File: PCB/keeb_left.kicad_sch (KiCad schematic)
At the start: 0 parts

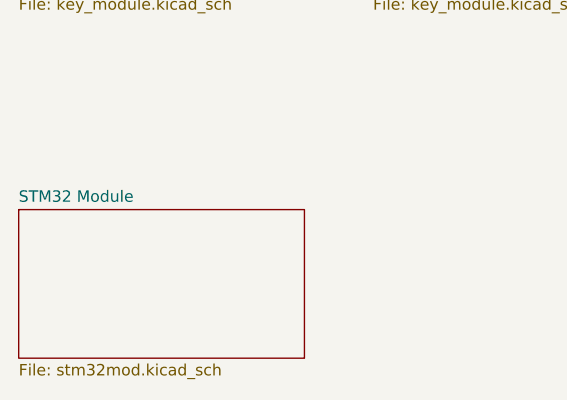
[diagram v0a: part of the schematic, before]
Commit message: Removed stm32, we're using a BluePill instead.
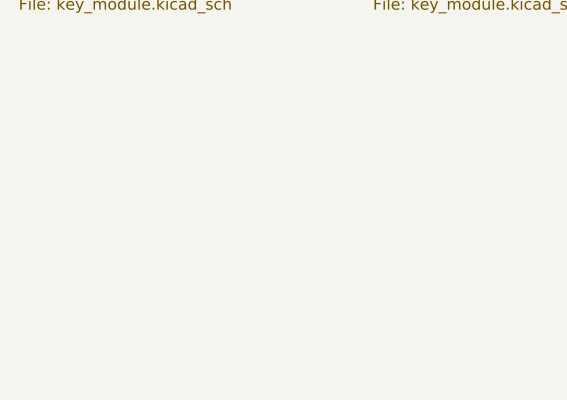
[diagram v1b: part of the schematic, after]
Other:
- removed sheet STM32 Module
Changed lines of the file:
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@@
-    )
-  )
-  (sheet (at 29.21 66.04) (size 31.75 16.51) (fields_autoplaced)
-    (stroke (width 0.1524) (type solid))
-    (fill (color 0 0 0 0.0000))
-    (property "Sheetname" "STM32 Module" (at 29.21 65.3284 0)
-      (effects (font (size 1.27 1.27)) (justify left bottom))
-    )
-    (property "Sheetfile" "stm32mod.kicad_sch" (at 29.21 83.1346 0)
-      (effects (font (size 1.27 1.27)) (justify left top))
-    )
-    (instances
-      (project "PCB"
-        (path "/d2f5552d-48c0-49b0-8e54-6764f47ed1da/5a7a16c1-b018-4a19-b382-77ab07b68c52" (page "54"))
-      )
     )
   )

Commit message: Done with STM32
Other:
- added sheet STM32 Module (stm32mod.kicad_sch)
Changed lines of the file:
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@@
+    (stroke (width 0) (type default))
+  )
+  (wire (pts (xy 49.53 81.28) (xy 25.4 81.28))
+    (stroke (width 0) (type default))
+  )
+  (wire (pts (xy 260.35 46.99) (xy 260.35 39.37))
     (stroke (width 0) (type default))
   )
@@
     (stroke (width 0) (type default))
   )
+  (wire (pts (xy 21.59 31.75) (xy 29.21 31.75))
+    (stroke (width 0) (type default))
+  )
+  (wire (pts (xy 25.4 81.28) (xy 25.4 46.99))
+    (stroke (width 0) (type default))
+  )
   (wire (pts (xy 60.96 31.75) (xy 68.58 31.75))
     (stroke (width 0) (type default))
@@
   )
   (wire (pts (xy 100.33 39.37) (xy 107.95 39.37))
+    (stroke (width 0) (type default))
+  )
+  (wire (pts (xy 21.59 86.36) (xy 21.59 31.75))
+    (stroke (width 0) (type default))
+  )
+  (wire (pts (xy 25.4 46.99) (xy 260.35 46.99))
+    (stroke (width 0) (type default))
+  )
+  (wire (pts (xy 49.53 86.36) (xy 21.59 86.36))
+    (stroke (width 0) (type default))
+  )
+  (wire (pts (xy 260.35 39.37) (xy 257.81 39.37))
     (stroke (width 0) (type default))
   )
@@
       )
     )
+  )
+  (sheet (at 49.53 67.31) (size 38.1 49.53) (fields_autoplaced)
+    (stroke (width 0.1524) (type solid))
+    (fill (color 0 0 0 0.0000))
+    (property "Sheetname" "STM32 Module" (at 49.53 66.5984 0)
+      (effects (font (size 1.27 1.27)) (justify left bottom))
+    )
+    (property "Sheetfile" "stm32mod.kicad_sch" (at 49.53 117.4246 0)
+      (effects (font (size 1.27 1.27)) (justify left top))
+    )
+    (pin "PA0" input (at 49.53 71.12 180)
+      (effects (font (size 1.27 1.27)) (justify left))
+    )
+    (pin "PB4" input (at 49.53 88.9 180)
+      (effects (font (size 1.27 1.27)) (justify left))
+    )
+    (pin "PB3" input (at 49.53 86.36 180)
+      (effects (font (size 1.27 1.27)) (justify left))
+    )
+    (pin "I2C2_SCL" input (at 87.63 83.82 0)
+      (effects (font (size 1.27 1.27)) (justify right))
+    )
+    (pin "I2C2_SDA" input (at 87.63 81.28 0)
+      (effects (font (size 1.27 1.27)) (justify right))
+    )
+    (pin "I2C1_SMBAI" input (at 87.63 76.2 0)
+      (effects (font (size 1.27 1.27)) (justify right))
+    )
+    (pin "PB9" input (at 49.53 93.98 180)
+      (effects (font (size 1.27 1.27)) (justify left))
+    )
+    (pin "PB14" input (at 49.53 99.06 180)
+      (effects (font (size 1.27 1.27)) (justify left))
+    )
+    (pin "PB13" input (at 49.53 96.52 180)
+      (effects (font (size 1.27 1.27)) (justify left))
+    )
+    (pin "PB15" input (at 49.53 101.6 180)
+      (effects (font (size 1.27 1.27)) (justify left))
+    )
+    (pin "I2C1_SCL" input (at 87.63 73.66 0)
+      (effects (font (size 1.27 1.27)) (justify right))
+    )
+    (pin "I2C1_SDA" input (at 87.63 71.12 0)
+      (effects (font (size 1.27 1.27)) (justify right))
+    )
+    (pin "PB8" input (at 49.53 91.44 180)
+      (effects (font (size 1.27 1.27)) (justify left))
+    )
+    (pin "PA15" input (at 49.53 81.28 180)
+      (effects (font (size 1.27 1.27)) (justify left))
+    )
+    (pin "USART1_RX" input (at 87.63 91.44 0)
+      (effects (font (size 1.27 1.27)) (justify right))
+    )
+    (pin "USART1_TX" input (at 87.63 93.98 0)
+      (effects (font (size 1.27 1.27)) (justify right))
+    )
+    (pin "USART1_CK" input (at 87.63 96.52 0)
+      (effects (font (size 1.27 1.27)) (justify right))
+    )
+    (pin "ADC12_IN6" input (at 49.53 111.76 180)
+      (effects (font (size 1.27 1.27)) (justify left))
+    )
+    (pin "ADC12_IN7" input (at 49.53 114.3 180)
+      (effects (font (size 1.27 1.27)) (justify left))
+    )
+    (pin "ADC12_IN4" input (at 49.53 106.68 180)
+      (effects (font (size 1.27 1.27)) (justify left))
+    )
+    (pin "ADC12_IN5" input (at 49.53 109.22 180)
+      (effects (font (size 1.27 1.27)) (justify left))
+    )
+    (pin "PA2" input (at 49.53 76.2 180)
+      (effects (font (size 1.27 1.27)) (justify left))
+    )
+    (pin "PA3" input (at 49.53 78.74 180)
+      (effects (font (size 1.27 1.27)) (justify left))
+    )
+    (pin "PA1" input (at 49.53 73.66 180)
+      (effects (font (size 1.27 1.27)) (justify left))
+    )
+    (pin "I2C2_SMBAI" input (at 87.63 86.36 0)
+      (effects (font (size 1.27 1.27)) (justify right))
+    )
+    (instances
+      (project "PCB"
+        (path "/d2f5552d-48c0-49b0-8e54-6764f47ed1da/5a7a16c1-b018-4a19-b382-77ab07b68c52" (page "54"))
+      )
+    )

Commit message: Ready to work on PCB
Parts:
- added D7: 6V ESD, footprint:SOD-123FL_L2.8-W1.8-LS3.7-BI, symbol JLCPCB:SMF6_0CA_C2990473
- added J1: ALS, Connector_PinHeader_2.54mm:PinHeader_1x03_P2.54mm_Vertical, symbol Connector_Generic:Conn_01x03
- added J1: Serial, Connector_PinHeader_2.54mm:PinHeader_1x05_P2.54mm_Vertical, symbol Connector_Generic:Conn_01x05
- added J1: I2C, Connector_PinHeader_2.54mm:PinHeader_1x04_P2.54mm_Vertical, symbol Connector_Generic:Conn_01x04
- added U44: TYPE-C-31-M-12, footprint:USB-C_SMD-TYPE-C-31-M-12, symbol JLCPCB:TYPE-C-31-M-12
- added U48: USBLC6-2SC6, Package_TO_SOT_SMD:SOT-23-6, symbol Power_Protection:USBLC6-2SC6
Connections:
- net STM32 Module/ADC12_IN4: now also J1.2 (Pin_2)
- net STM32 Module/I2C2_SCL: now also J1.3 (Pin_3)
- net STM32 Module/I2C2_SDA: now also J1.2 (Pin_2)
- net STM32 Module/USART1_CK: now also J1.4 (Pin_4)
- net STM32 Module/USART1_RX: now also J1.2 (Pin_2)
- net STM32 Module/USART1_TX: now also J1.3 (Pin_3)
- new net +5V: J1.3 (Pin_3), U48.5 (VBUS)
- new net GND: D7.1, J1.1 (Pin_1), J1.4 (Pin_4), J1.5 (Pin_5), U44.0 (SH), U44.A1 (GND), U44.A12 (GND), U44.B1 (GND), U44.B12 (GND), U48.2 (GND)
- new net HALF_CONN_C: U44.A5 (CC1), U44.B5 (CC2)
- new net HALF_CONN_N: U44.A7 (DN1), U44.B7 (DN2), U48.1 (I/O1)
- new net HALF_CONN_P: U44.A6 (DP1), U44.B6 (DP2), U48.3 (I/O2)
- new net HALF_CONN_S: U44.A8 (SBU1), U44.B8 (SBU2)
- new net HALF_SCL: U48.4 (I/O2)
- new net HALF_SDA: U48.6 (I/O1)
- new net VBUS: D7.2, J1.1 (Pin_1), J1.1 (Pin_1), U44.A4 (VBUS), U44.A9 (VBUS), U44.B4 (VBUS), U44.B9 (VBUS)
- no-connect marks 0 -> 6
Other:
- sheet STM32 Module ports: added VUSB_RAW; removed none

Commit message: Plugin works.
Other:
- added sheet 5-Key Module1 (key_module_5.kicad_sch)
- note added: "Left-Right Connector"
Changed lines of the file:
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@@
     (stroke (width 0) (type default))
+  )
+  (text "Left-Right Connector" (at 20.32 133.35 0)
+    (effects (font (size 1.27 1.27)) (justify left bottom))
   )
   (label "HALF_CONN_C" (at 24.13 162.56 0) (fields_autoplaced)
@@
         )
         (path "/d2f5552d-48c0-49b0-8e54-6764f47ed1da/5a7a16c1-b018-4a19-b382-77ab07b68c52"
-          (reference "#PWR0227") (unit 1)
+          (reference "#PWR060008") (unit 1)
         )
       )
@@
         )
         (path "/d2f5552d-48c0-49b0-8e54-6764f47ed1da/5a7a16c1-b018-4a19-b382-77ab07b68c52"
-          (reference "#PWR0211") (unit 1)
+          (reference "#PWR060007") (unit 1)
         )
       )
@@
   (symbol (lib_id "power:+5V") (at 114.3 165.1 0) (unit 1)
     (in_bom yes) (on_board yes) (dnp no)
-    (property "Reference" "#PWR0230" (at 114.3 168.91 0)
+    (property "Reference" "#PWR060013" (at 114.3 168.91 0)
       (effects (font (size 1.27 1.27)) hide)
     )
@@
       (project "PCB"
         (path "/d2f5552d-48c0-49b0-8e54-6764f47ed1da/5a7a16c1-b018-4a19-b382-77ab07b68c52"
-          (reference "#PWR0230") (unit 1)
+          (reference "#PWR060013") (unit 1)
         )
       )
@@
   (symbol (lib_id "power:+5V") (at 27.94 101.6 0) (unit 1)
     (in_bom yes) (on_board yes) (dnp no) (fields_autoplaced)
-    (property "Reference" "#PWR0236" (at 27.94 105.41 0)
+    (property "Reference" "#PWR060001" (at 27.94 105.41 0)
       (effects (font (size 1.27 1.27)) hide)
     )
@@
       (project "PCB"
         (path "/d2f5552d-48c0-49b0-8e54-6764f47ed1da/5a7a16c1-b018-4a19-b382-77ab07b68c52"
-          (reference "#PWR0236") (unit 1)
+          (reference "#PWR060001") (unit 1)
         )
       )
@@
         )
         (path "/d2f5552d-48c0-49b0-8e54-6764f47ed1da/5a7a16c1-b018-4a19-b382-77ab07b68c52"
-          (reference "#PWR0229") (unit 1)
+          (reference "#PWR060010") (unit 1)
         )
       )
@@
         )
         (path "/d2f5552d-48c0-49b0-8e54-6764f47ed1da/5a7a16c1-b018-4a19-b382-77ab07b68c52"
-          (reference "#PWR0232") (unit 1)
+          (reference "#PWR060005") (unit 1)
         )
       )
@@
         )
         (path "/d2f5552d-48c0-49b0-8e54-6764f47ed1da/5a7a16c1-b018-4a19-b382-77ab07b68c52"
-          (reference "D3") (unit 1)
+          (reference "D60001") (unit 1)
         )
       )
@@
         )
         (path "/d2f5552d-48c0-49b0-8e54-6764f47ed1da/5a7a16c1-b018-4a19-b382-77ab07b68c52"
-          (reference "#PWR0235") (unit 1)
+          (reference "#PWR060012") (unit 1)
         )
       )
@@
         )
         (path "/d2f5552d-48c0-49b0-8e54-6764f47ed1da/5a7a16c1-b018-4a19-b382-77ab07b68c52"
-          (reference "#PWR0210") (unit 1)
+          (reference "#PWR060004") (unit 1)
         )
       )
@@
         )
         (path "/d2f5552d-48c0-49b0-8e54-6764f47ed1da/5a7a16c1-b018-4a19-b382-77ab07b68c52"
-          (reference "J3") (unit 1)
+          (reference "J60001") (unit 1)
         )
       )
@@
         )
         (path "/d2f5552d-48c0-49b0-8e54-6764f47ed1da/5a7a16c1-b018-4a19-b382-77ab07b68c52"
-          (reference "J4") (unit 1)
+          (reference "J60002") (unit 1)
         )
       )
@@
         )
         (path "/d2f5552d-48c0-49b0-8e54-6764f47ed1da/5a7a16c1-b018-4a19-b382-77ab07b68c52"
-          (reference "J2") (unit 1)
+          (reference "J60003") (unit 1)
         )
       )
@@
         )
         (path "/d2f5552d-48c0-49b0-8e54-6764f47ed1da/5a7a16c1-b018-4a19-b382-77ab07b68c52"
-          (reference "#PWR0231") (unit 1)
+          (reference "#PWR060009") (unit 1)
         )
       )
@@
         )
         (path "/d2f5552d-48c0-49b0-8e54-6764f47ed1da/5a7a16c1-b018-4a19-b382-77ab07b68c52"
-          (reference "#PWR0234") (unit 1)
+          (reference "#PWR060002") (unit 1)
         )
       )
@@
         )
         (path "/d2f5552d-48c0-49b0-8e54-6764f47ed1da/5a7a16c1-b018-4a19-b382-77ab07b68c52"
-          (reference "U50") (unit 1)
+          (reference "U60002") (unit 1)
         )
       )
@@
         )
         (path "/d2f5552d-48c0-49b0-8e54-6764f47ed1da/5a7a16c1-b018-4a19-b382-77ab07b68c52"
-          (reference "U49") (unit 1)
+          (reference "U60001") (unit 1)
         )
       )
@@
         )
         (path "/d2f5552d-48c0-49b0-8e54-6764f47ed1da/5a7a16c1-b018-4a19-b382-77ab07b68c52"
-          (reference "#PWR0209") (unit 1)
+          (reference "#PWR060003") (unit 1)
         )
       )
@@
         )
         (path "/d2f5552d-48c0-49b0-8e54-6764f47ed1da/5a7a16c1-b018-4a19-b382-77ab07b68c52"
-          (reference "#PWR0233") (unit 1)
+          (reference "#PWR060006") (unit 1)
         )
       )
@@
         )
         (path "/d2f5552d-48c0-49b0-8e54-6764f47ed1da/5a7a16c1-b018-4a19-b382-77ab07b68c52"
-          (reference "#PWR0237") (unit 1)
+          (reference "#PWR060011") (unit 1)
         )
       )
@@
       )
     )
+  )
+  (sheet (at 205.74 80.01) (size 31.75 12.7) (fields_autoplaced)
+    (stroke (width 0.1524) (type solid))
+    (fill (color 0 0 0 0.0000))
+    (property "Sheetname" "5-Key Module1" (at 205.74 79.2984 0)
+      (effects (font (size 1.27 1.27)) (justify left bottom))
+    )
+    (property "Sheetfile" "key_module_5.kicad_sch" (at 205.74 93.2946 0)
+      (effects (font (size 1.27 1.27)) (justify left top))
+    )
+    (pin "SR_IN" input (at 205.74 90.17 180)
+      (effects (font (size 1.27 1.27)) (justify left))
+    )
+    (pin "SR_CLOCK" input (at 222.25 80.01 90)
+      (effects (font (size 1.27 1.27)) (justify right))
+    )
+    (pin "SR_LOAD" input (at 219.71 80.01 90)
+      (effects (font (size 1.27 1.27)) (justify right))
+    )
+    (pin "LEDInput" input (at 205.74 82.55 180)
+      (effects (font (size 1.27 1.27)) (justify left))
+    )
+    (pin "SR_OUT" input (at 237.49 90.17 0)
+      (effects (font (size 1.27 1.27)) (justify right))
+    )
+    (pin "LEDOutput" input (at 237.49 82.55 0)
+      (effects (font (size 1.27 1.27)) (justify right))
+    )
+    (instances
+      (project "PCB"
+        (path "/d2f5552d-48c0-49b0-8e54-6764f47ed1da" (page "47"))
+        (path "/d2f5552d-48c0-49b0-8e54-6764f47ed1da/5a7a16c1-b018-4a19-b382-77ab07b68c52" (page "49"))
+      )
+    )

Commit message: Laying out the PCB.
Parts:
- removed J1: Serial, Connector_PinHeader_2.54mm:PinHeader_1x05_P2.54mm_Vertical, symbol Connector_Generic:Conn_01x05
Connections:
- no-connect marks 6 -> 9
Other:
- removed sheet 5-Key Module1
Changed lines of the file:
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@@
   (junction (at 125.73 22.86) (diameter 0) (color 0 0 0 0)
   )
+  (no_connect (at 87.63 93.98))
   (no_connect (at 81.28 170.18))
   (no_connect (at 87.63 86.36))
   (no_connect (at 87.63 76.2))
+  (no_connect (at 87.63 91.44))
   (no_connect (at 257.81 31.75))
+  (no_connect (at 87.63 96.52))
   (no_connect (at 29.21 39.37))
   (no_connect (at 81.28 162.56))
@@
     (stroke (width 0) (type default))
   )
-  (wire (pts (xy 90.17 88.9) (xy 95.25 88.9))
-    (stroke (width 0) (type default))
-  )
   (wire (pts (xy 71.12 172.72) (xy 63.5 172.72))
     (stroke (width 0) (type default))
@@
     (stroke (width 0) (type default))
   )
-  (wire (pts (xy 87.63 96.52) (xy 95.25 96.52))
-    (stroke (width 0) (type default))
-  )
   (wire (pts (xy 25.4 81.28) (xy 25.4 46.99))
     (stroke (width 0) (type default))
@@
     (stroke (width 0) (type default))
   )
-  (wire (pts (xy 87.63 91.44) (xy 95.25 91.44))
-    (stroke (width 0) (type default))
-  )
   (wire (pts (xy 29.21 160.02) (xy 40.64 160.02))
     (stroke (width 0) (type default))
@@
   )
   (wire (pts (xy 86.36 22.86) (xy 46.99 22.86))
-    (stroke (width 0) (type default))
-  )
-  (wire (pts (xy 87.63 93.98) (xy 95.25 93.98))
     (stroke (width 0) (type default))
   )
@@
   )
   (label "HALF_CONN_P" (at 24.13 165.1 0) (fields_autoplaced)
-    (effects (font (size 1.27 1.27)) (justify left bottom))
-  )
-  (label "VBUS" (at 90.17 88.9 0) (fields_autoplaced)
     (effects (font (size 1.27 1.27)) (justify left bottom))
   )
@@
         (path "/d2f5552d-48c0-49b0-8e54-6764f47ed1da/5a7a16c1-b018-4a19-b382-77ab07b68c52"
           (reference "J60001") (unit 1)
-        )
-      )
-    )
-  )
-  (symbol (lib_id "Connector_Generic:Conn_01x05") (at 100.33 93.98 0) (unit 1)
-    (in_bom yes) (on_board yes) (dnp no) (fields_autoplaced)
-    (property "Reference" "J1" (at 102.87 92.71 0)
-      (effects (font (size 1.27 1.27)) (justify left))
-    )
-    (property "Value" "Serial" (at 102.87 95.25 0)
-      (effects (font (size 1.27 1.27)) (justify left))
-    )
-    (property "Footprint" "Connector_PinHeader_2.54mm:PinHeader_1x05_P2.54mm_Vertical" (at 100.33 93.98 0)
-      (effects (font (size 1.27 1.27)) hide)
-    )
-    (property "Datasheet" "~" (at 100.33 93.98 0)
-      (effects (font (size 1.27 1.27)) hide)
-    )
-    (pin "1")
-    (pin "2")
-    (pin "3")
-    (pin "4")
-    (pin "5")
-    (instances
-      (project "PCB"
-        (path "/d2f5552d-48c0-49b0-8e54-6764f47ed1da/5a7a16c1-b018-4a19-b382-77ab07b68c52/2030ad47-566c-4a6b-b217-7789d857619d"
-          (reference "J1") (unit 1)
-        )
-        (path "/d2f5552d-48c0-49b0-8e54-6764f47ed1da/5a7a16c1-b018-4a19-b382-77ab07b68c52"
-          (reference "J60002") (unit 1)
         )
       )
@@
     )
   )
-  (symbol (lib_id "power:GND") (at 95.25 99.06 0) (unit 1)
-    (in_bom yes) (on_board yes) (dnp no)
-    (property "Reference" "#PWR0225" (at 95.25 105.41 0)
-      (effects (font (size 1.27 1.27)) hide)
-    )
-    (property "Value" "GND" (at 95.25 102.87 0)
-      (effects (font (size 1.27 1.27)))
-    )
-    (property "Footprint" "" (at 95.25 99.06 0)
-      (effects (font (size 1.27 1.27)) hide)
-    )
-    (property "Datasheet" "" (at 95.25 99.06 0)
-      (effects (font (size 1.27 1.27)) hide)
-    )
-    (pin "1")
-    (instances
-      (project "PCB"
-        (path "/d2f5552d-48c0-49b0-8e54-6764f47ed1da/5a7a16c1-b018-4a19-b382-77ab07b68c52/2030ad47-566c-4a6b-b217-7789d857619d"
-          (reference "#PWR0225") (unit 1)
-        )
-        (path "/d2f5552d-48c0-49b0-8e54-6764f47ed1da/5a7a16c1-b018-4a19-b382-77ab07b68c52"
-          (reference "#PWR060011") (unit 1)
-        )
-      )
-    )
-  )
   (sheet (at 186.69 29.21) (size 31.75 12.7) (fields_autoplaced)
     (stroke (width 0.1524) (type solid))
@@
       )
     )
-  )
-  (sheet (at 205.74 80.01) (size 31.75 12.7) (fields_autoplaced)
-    (stroke (width 0.1524) (type solid))
-    (fill (color 0 0 0 0.0000))
-    (property "Sheetname" "5-Key Module1" (at 205.74 79.2984 0)
-      (effects (font (size 1.27 1.27)) (justify left bottom))
-    )
-    (property "Sheetfile" "key_module_5.kicad_sch" (at 205.74 93.2946 0)
-      (effects (font (size 1.27 1.27)) (justify left top))
-    )
-    (pin "SR_IN" input (at 205.74 90.17 180)
-      (effects (font (size 1.27 1.27)) (justify left))
-    )
-    (pin "SR_CLOCK" input (at 222.25 80.01 90)
-      (effects (font (size 1.27 1.27)) (justify right))
-    )
-    (pin "SR_LOAD" input (at 219.71 80.01 90)
-      (effects (font (size 1.27 1.27)) (justify right))
-    )
-    (pin "LEDInput" input (at 205.74 82.55 180)
-      (effects (font (size 1.27 1.27)) (justify left))
-    )
-    (pin "SR_OUT" input (at 237.49 90.17 0)
-      (effects (font (size 1.27 1.27)) (justify right))
-    )
-    (pin "LEDOutput" input (at 237.49 82.55 0)
-      (effects (font (size 1.27 1.27)) (justify right))
-    )
-    (instances
-      (project "PCB"
-        (path "/d2f5552d-48c0-49b0-8e54-6764f47ed1da" (page "47"))
-        (path "/d2f5552d-48c0-49b0-8e54-6764f47ed1da/5a7a16c1-b018-4a19-b382-77ab07b68c52" (page "49"))
-      )
-    )

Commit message: Removed 8-key units, now using the PCB view to handle routing the keys to the SOIP shift registers.
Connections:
- no-connect marks 9 -> 8
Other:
- removed sheet 5-Key Module
- added sheet 8-Key Module5 (key_module.kicad_sch)
- added sheet Key Unit0 (key_column.kicad_sch)
- added sheet Key Unit1 (key_column.kicad_sch)
- added sheet Key Unit11 (key_column.kicad_sch)
- added sheet Key Unit14 (key_column.kicad_sch)
- added sheet Key Unit15 (key_column.kicad_sch)
- added sheet Key Unit16 (key_column.kicad_sch)
- added sheet Key Unit17 (key_column.kicad_sch)
- added sheet Key Unit18 (key_column.kicad_sch)
- added sheet Key Unit19 (key_column.kicad_sch)
- added sheet Key Unit2 (key_column.kicad_sch)
- added sheet Key Unit20 (key_column.kicad_sch)
- added sheet Key Unit21 (key_column.kicad_sch)
- added sheet Key Unit22 (key_column.kicad_sch)
- added sheet Key Unit23 (key_column.kicad_sch)
- added sheet Key Unit24 (key_column.kicad_sch)
- added sheet Key Unit25 (key_column.kicad_sch)
- added sheet Key Unit26 (key_column.kicad_sch)
- added sheet Key Unit27 (key_column.kicad_sch)
- added sheet Key Unit28 (key_column.kicad_sch)
- added sheet Key Unit29 (key_column.kicad_sch)
- added sheet Key Unit3 (key_column.kicad_sch)
- added sheet Key Unit30 (key_column.kicad_sch)
- added sheet Key Unit31 (key_column.kicad_sch)
- added sheet Key Unit32 (key_column.kicad_sch)
- added sheet Key Unit33 (key_column.kicad_sch)
- added sheet Key Unit34 (key_column.kicad_sch)
- added sheet Key Unit35 (key_column.kicad_sch)
- added sheet Key Unit36 (key_column.kicad_sch)
- added sheet Key Unit37 (key_column.kicad_sch)
- added sheet Key Unit38 (key_column.kicad_sch)
- added sheet Key Unit39 (key_column.kicad_sch)
- added sheet Key Unit4 (key_column.kicad_sch)
- added sheet Key Unit40 (key_column.kicad_sch)
- added sheet Key Unit41 (key_column.kicad_sch)
- added sheet Key Unit42 (key_column.kicad_sch)
- added sheet Key Unit43 (key_column.kicad_sch)
- added sheet Key Unit44 (key_column.kicad_sch)
- added sheet Key Unit45 (key_column.kicad_sch)
- added sheet Key Unit47 (key_column.kicad_sch)
- added sheet Key Unit49 (key_column.kicad_sch)
- added sheet Key Unit5 (key_column.kicad_sch)
- added sheet Key Unit50 (key_column.kicad_sch)
- added sheet Key Unit51 (key_column.kicad_sch)
- added sheet Key Unit6 (key_column.kicad_sch)
- added sheet Key Unit7 (key_column.kicad_sch)
- sheet 8-Key Module ports: added none; removed LEDInput, LEDOutput
- sheet 8-Key Module1 ports: added none; removed LEDInput, LEDOutput
- sheet 8-Key Module2 ports: added none; removed LEDInput, LEDOutput
- sheet 8-Key Module3 ports: added none; removed LEDInput, LEDOutput
- sheet 8-Key Module4 ports: added none; removed LEDInput, LEDOutput

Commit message: Updated schematics for KiCAD 8
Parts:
- renumbered D7 to D60001, J1 to J60001, J1 to J60003, U44 to U60001, U48 to U60002
